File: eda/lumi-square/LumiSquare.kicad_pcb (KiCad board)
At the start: 2 copper layers, 87.2 x 87.2 mm, 105 parts, among them J1 USB_C_Receptacle_USB2.0_14P, J2 Conn_01x12, J3 Conn_01x12, J4 Conn_01x02, J7 FTSH-105-01-X-DV-P-K-X, Q1 IRLML6244, Q10 IRLML2246, Q15 TSM680P06CH, Q16 TSM680P06CH, Q17 TSM680P06CH, Q18 TSM680P06CH, Q2 IRLML2246, Q3 IRLML2246, Q4 MMBT3904, Q5 MMBT3904, Q6 MMBT3904, Q7 MMBT3904, Q8 MMBT3904, Q9 MMBT3904, SW1 SW_SPST, SW2 SW_Push, SW3 SW_Push, SW4 SW_Push, SW5 SW_Push, U1 MCP73831-2-OT, U2 TPS3840, U3 TLV61070A, U4 TLV61070A, U5 ATSAMD21J18A-A, U6 STP16CPC05MTR, U7 CM1224-02SR, U8 MIC5225-3.3YM5, U9 DFR0299

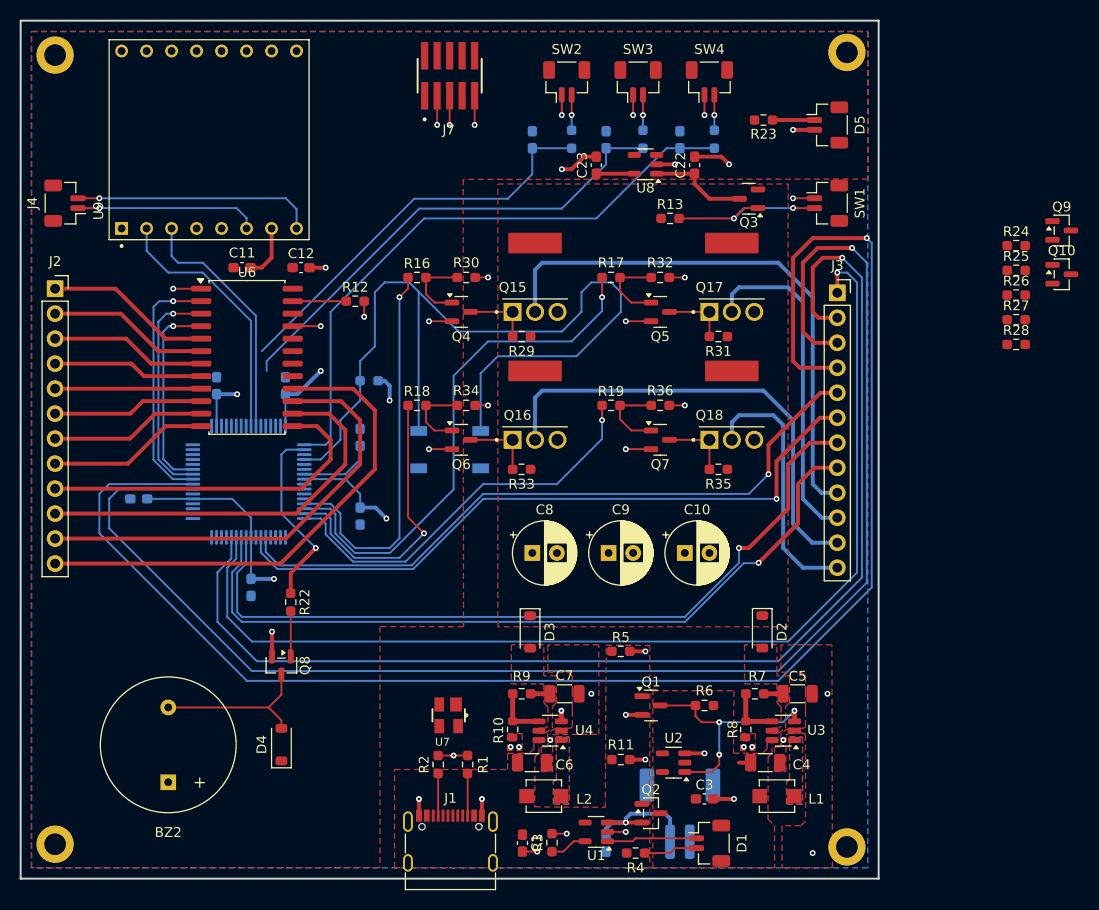
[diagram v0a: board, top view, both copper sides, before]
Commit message: Removed usb connection components and finished circuit
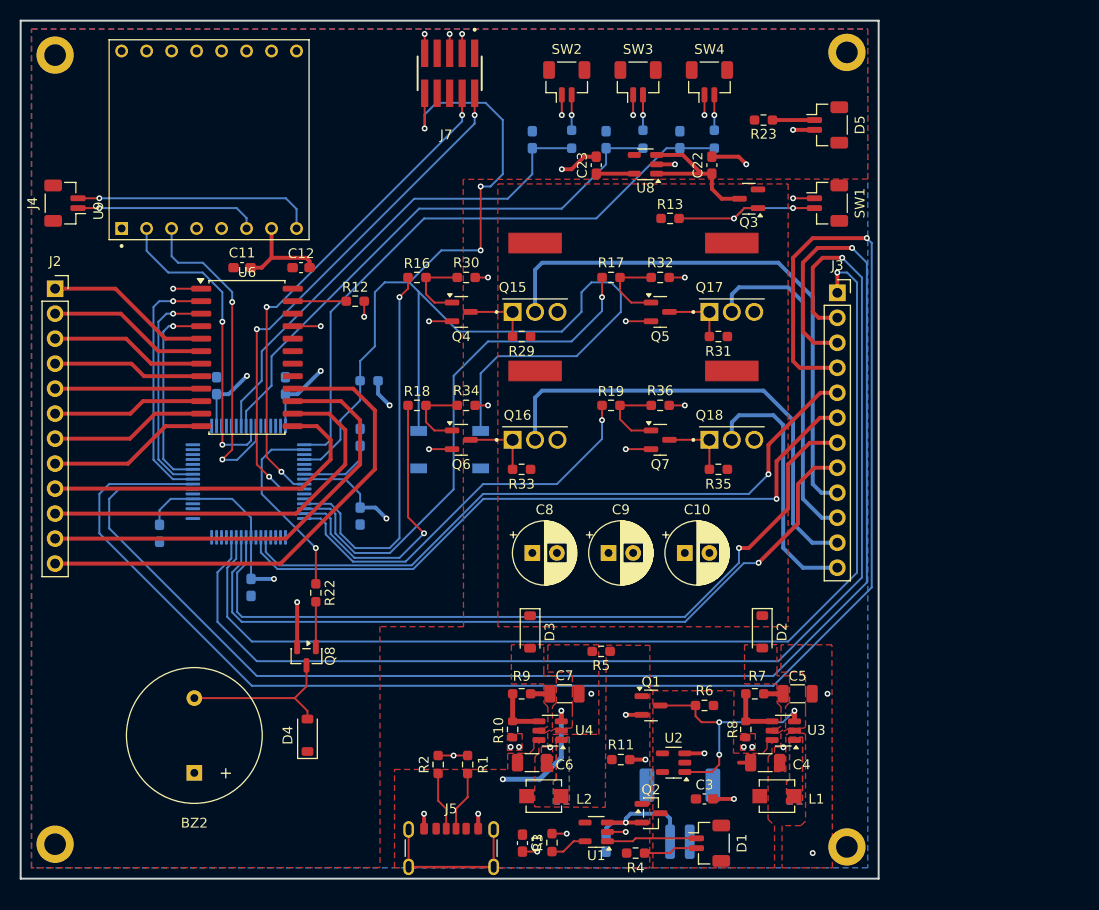
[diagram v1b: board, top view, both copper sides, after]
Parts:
- removed J1: USB_C_Receptacle_USB2.0_14P, Connector_USB:USB_C_Receptacle_G-Switch_GT-USB-7010ASV
- removed Q10: IRLML2246, Package_TO_SOT_SMD:SOT-23
- removed Q9: MMBT3904, Package_TO_SOT_SMD:SOT-23
- removed R24, R25: 1.3k, Resistor_SMD:R_0603_1608Metric_Pad0.98x0.95mm_HandSolder
- removed R26: 33k, Resistor_SMD:R_0603_1608Metric_Pad0.98x0.95mm_HandSolder
- removed R27: 41k, Resistor_SMD:R_0603_1608Metric_Pad0.98x0.95mm_HandSolder
- removed R28: 100k, Resistor_SMD:R_0603_1608Metric_Pad0.98x0.95mm_HandSolder
- removed U7: CM1224-02SR, CM1224-02SR:SOT143
- added J5: USB_C_Receptacle_PowerOnly_6P, Connector_USB:USB_C_Receptacle_GCT_USB4125-xx-x-0190_6P_TopMnt_Horizontal, F.Cu at (144.8, 143.6)
- moved C18 4.09 mm to (115.1, 110.5), turned to -90 degrees
- moved BZ2 2.82 mm to (118.7, 131.1)
- moved D4 2.82 mm to (130.2, 131.0)
- moved Q8 2.72 mm to (130.1, 123.0)
- moved R22 2.72 mm to (131.0, 116.5)
- moved R5 2.00 mm to (160.0, 122.5), turned to 180 degrees
- moved C22 1.75 mm to (171.2, 73.1)
- moved J7 0.25 mm to (144.6, 63.8), turned to 180 degrees
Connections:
- U5 pad 31: /PA14 USB VBUS -> unconnected-(U5-PA14-Pad31)
- U5 pad 45: /TARGET USB N -> unconnected-(U5-PA24-Pad45)
- U5 pad 46: /TARGET USB P -> unconnected-(U5-PA25-Pad46)
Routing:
- net /SWDIO: track 0.00 -> 52.2 mm, vias 0 -> 3
- net /SWCLK: track 0.00 -> 49.5 mm, vias 0 -> 3
- net /Reset Pin: track 90.9 -> 127.2 mm, vias 0 -> 3
- net unconnected-(J5-SHIELD-PadSH): track 0.00 -> 16.2 mm
- net /5V USB: track 1.08 -> 12.7 mm, vias 1 -> 2
- net /MCU RX: track 25.1 -> 33.7 mm, vias 0 -> 2
- net /Previous Btn: track 41.6 -> 50.0 mm
- net Net-(Q3-D): track 10.1 -> 16.8 mm
- net /Next Btn: track 49.2 -> 55.6 mm
- net /MCU TX: track 26.5 -> 31.8 mm, vias 0 -> 2
- net +3.3V Main: track 50.7 -> 52.9 mm
- net Net-(J5-CC2): track 4.29 -> 6.10 mm
- net Net-(J5-CC1): track 4.29 -> 5.95 mm
- net /Buzzer PWM: track 19.1 -> 19.7 mm
- net GNDREF: track 81.5 -> 81.6 mm, vias 44 -> 42

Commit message: Fixed warnings
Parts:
- J4: footprint Connector_JST:JST_SH_BM02B-SRSS-TB_1x02-1MP_P1.00mm_Vertical -> Connector_JST:JST_SH_SM02B-SRSS-TB_1x02-1MP_P1.00mm_Horizontal; moved to B.Cu
- moved J4 30.6 mm to (135.5, 70.8), turned to -90 degrees
- moved J7 0.75 mm to (144.6, 64.5), turned to 0 degrees
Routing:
- net /Speaker-: track 24.6 -> 11.3 mm, vias 1 -> 0
- net GNDREF: track 81.6 -> 91.7 mm
- net /SWCLK: track 49.5 -> 57.2 mm
- net /SWDIO: track 52.2 -> 58.8 mm
- net /Speaker+: track 18.6 -> 16.3 mm, vias 1 -> 0
- net /Reset Pin: track 127.2 -> 126.2 mm
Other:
- board text added: "QB.Creates"
- board text added: "pcb-lumisquare-A1"

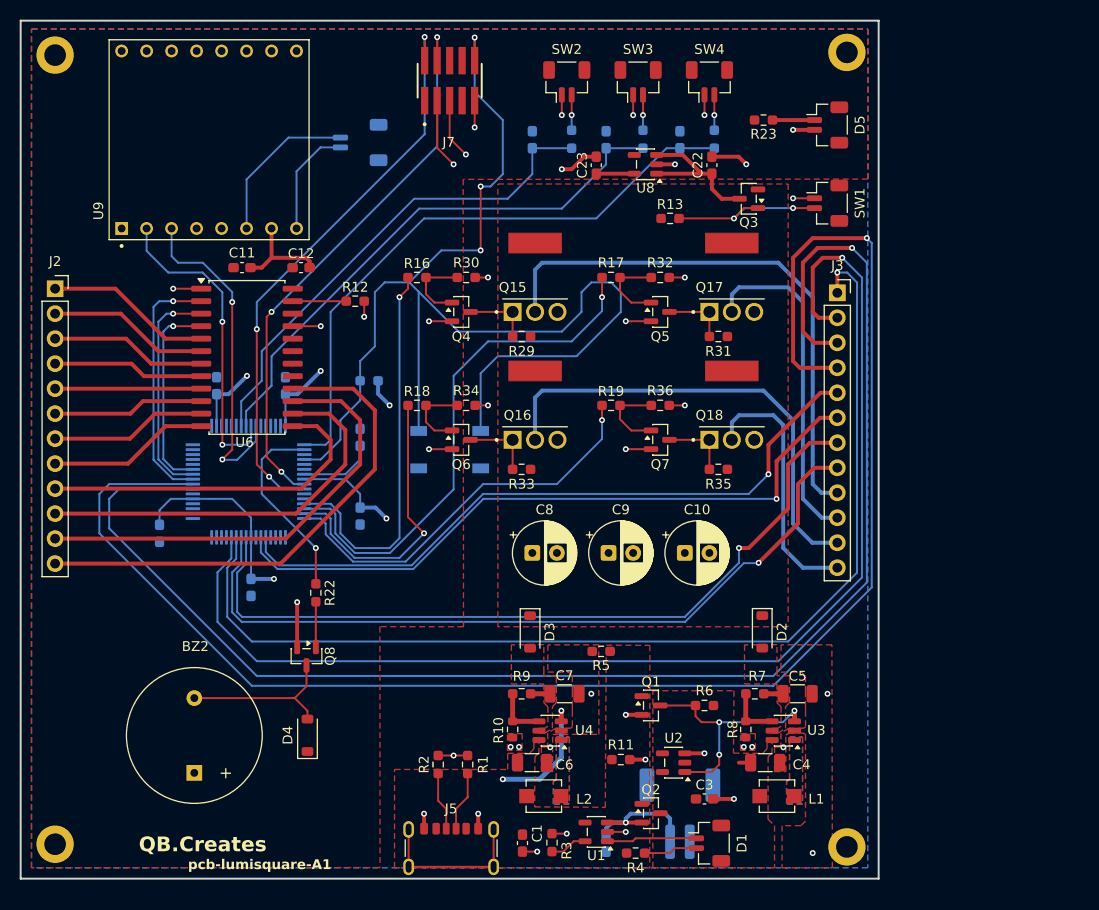
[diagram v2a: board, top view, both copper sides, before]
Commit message: Fixed header positions
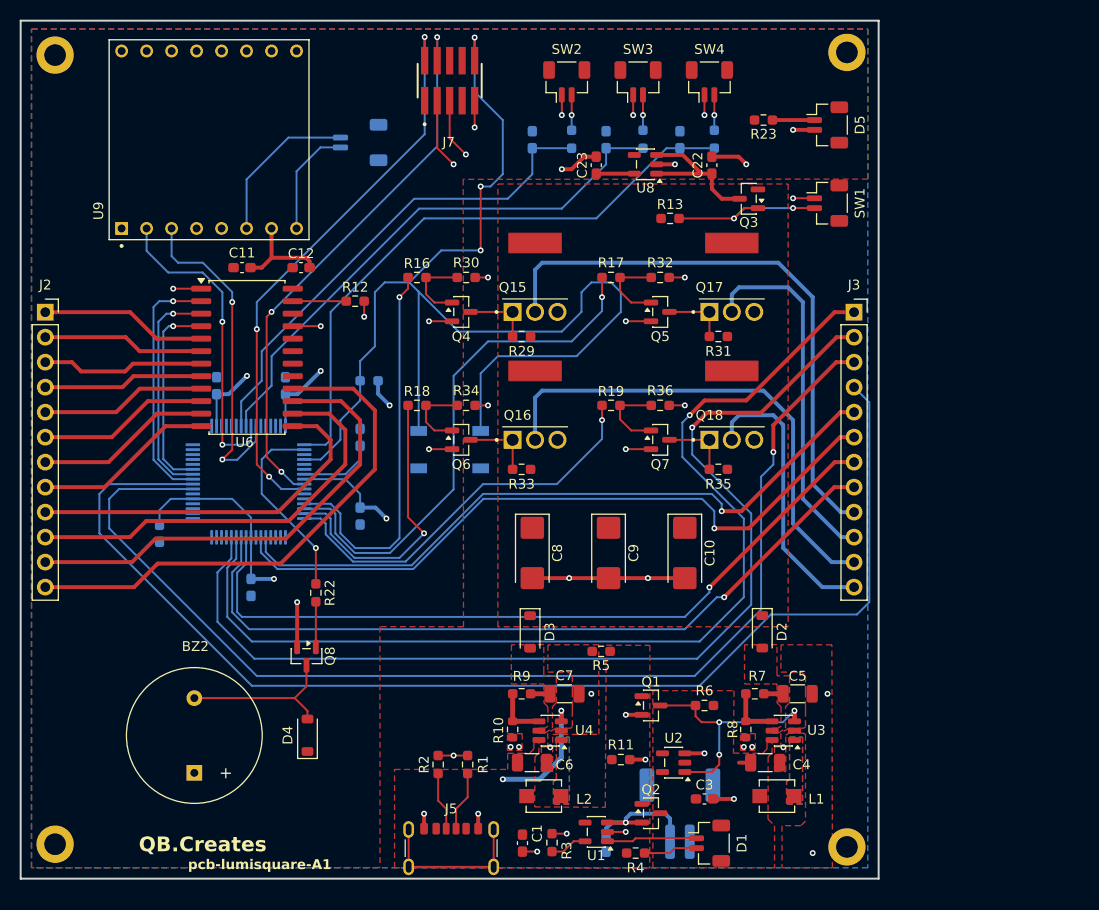
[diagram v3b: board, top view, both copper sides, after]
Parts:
- C10, C8, C9: footprint Capacitor_THT:CP_Radial_D6.3mm_P2.50mm -> Capacitor_Tantalum_SMD:CP_EIA-6032-28_Kemet-C_HandSolder
- moved J3 2.60 mm to (185.7, 88.0)
- moved J2 2.59 mm to (103.5, 88.0)
- turned C10 to -90 degrees
- turned C8 to -90 degrees
- turned C9 to -90 degrees
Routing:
- net /Row/Input 4: track 162.3 -> 124.6 mm, vias 1 -> 0
- net /Row/Input 3: track 150.3 -> 117.3 mm
- net /Row/Input 2: track 123.8 -> 108.0 mm
- net GNDREF: track 91.7 -> 107.2 mm, vias 42 -> 44
- net /Row/Input 1: track 110.4 -> 106.3 mm
- net /Col 3 Anode: track 47.9 -> 50.4 mm
- net /Col 2 Anode: track 34.2 -> 36.7 mm
- net /Col 4 Anode: track 26.5 -> 29.1 mm
- net /Col 1 Anode: track 56.1 -> 58.6 mm
- net /Col/Output 3: track 80.0 -> 77.7 mm
- net Net-(J2-Pin_12): track 51.7 -> 54.0 mm
- net /Col/Output 2: track 69.4 -> 71.6 mm
- net Net-(J2-Pin_11): track 46.3 -> 48.3 mm
- net Net-(J2-Pin_9): track 35.7 -> 37.6 mm
- net Net-(J2-Pin_8): track 16.4 -> 18.4 mm
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
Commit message: Added test points
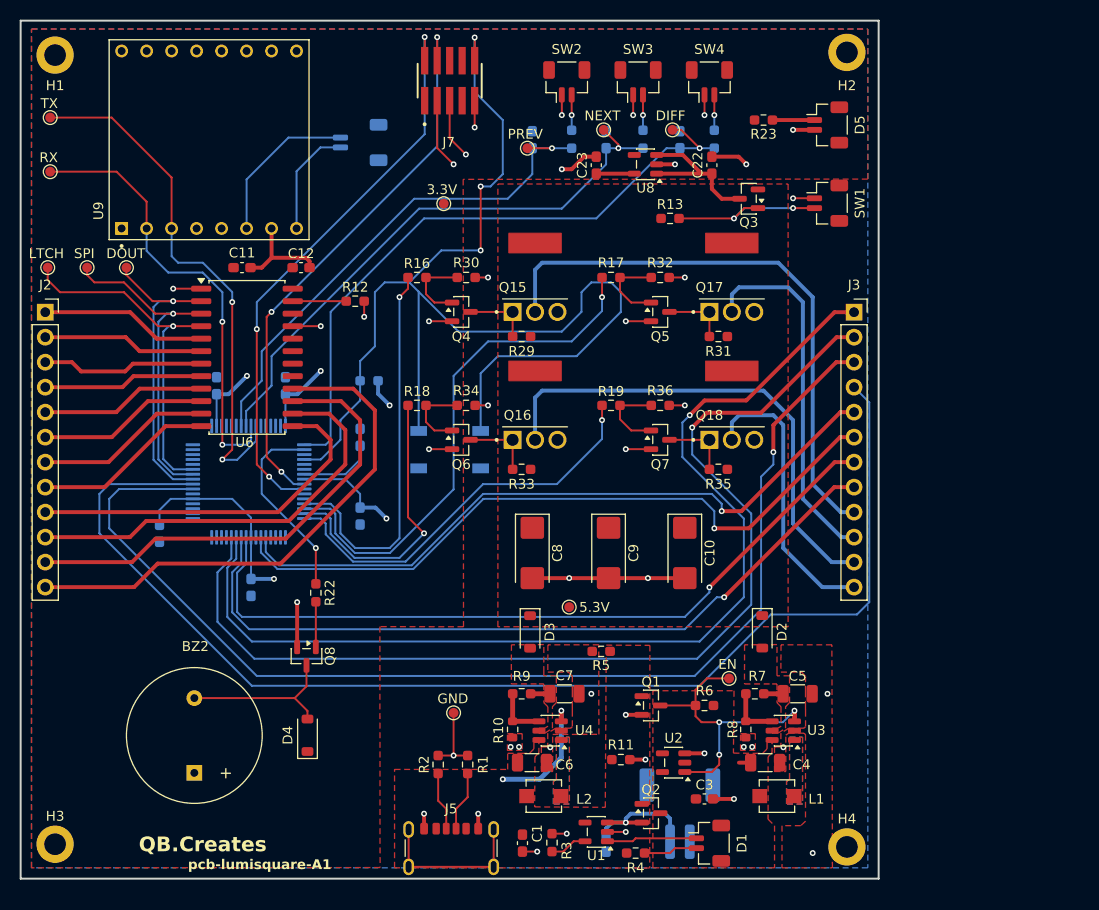
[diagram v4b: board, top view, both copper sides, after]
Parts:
- removed REF** (x4): M2, MountingHole:MountingHole_2.2mm_M2_DIN965_Pad
- added H1: MountingHole, MountingHole:MountingHole_2.2mm_M2_DIN965_Pad, F.Cu at (104.5, 61.9)
- added H2: MountingHole, MountingHole:MountingHole_2.2mm_M2_DIN965_Pad, F.Cu at (185.0, 61.6)
- added H3: MountingHole, MountingHole:MountingHole_2.2mm_M2_DIN965_Pad, F.Cu at (104.5, 142.1)
- added H4: MountingHole, MountingHole:MountingHole_2.2mm_M2_DIN965_Pad, F.Cu at (185.0, 142.4)
- added J1: Conn_01x01, TestPoint:TestPoint_Pad_D1.0mm, F.Cu at (156.8, 118.0)
- added J10: Conn_01x01, TestPoint:TestPoint_Pad_D1.0mm, F.Cu at (152.5, 71.4)
- added J11: Conn_01x01, TestPoint:TestPoint_Pad_D1.0mm, F.Cu at (160.2, 69.5)
- added J12: Conn_01x01, TestPoint:TestPoint_Pad_D1.0mm, F.Cu at (167.2, 69.5)
- added J13: Conn_01x01, TestPoint:TestPoint_Pad_D1.0mm, F.Cu at (104.0, 73.8)
- added J14: Conn_01x01, TestPoint:TestPoint_Pad_D1.0mm, F.Cu at (104.0, 68.2)
- added J15: Conn_01x01, TestPoint:TestPoint_Pad_D1.0mm, F.Cu at (111.8, 83.5)
- added J16: Conn_01x01, TestPoint:TestPoint_Pad_D1.0mm, F.Cu at (107.8, 83.5)
- added J17: Conn_01x01, TestPoint:TestPoint_Pad_D1.0mm, F.Cu at (103.8, 83.5)
- added J6: Conn_01x01, TestPoint:TestPoint_Pad_D1.0mm, F.Cu at (173.0, 125.2)
- added J8: Conn_01x01, TestPoint:TestPoint_Pad_D1.0mm, F.Cu at (145.0, 128.8)
- added J9: Conn_01x01, TestPoint:TestPoint_Pad_D1.0mm, F.Cu at (144.0, 77.0)
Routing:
- net /MCU RX: track 33.7 -> 53.7 mm
- net /SPI Latch: track 20.5 -> 36.4 mm
- net /MCU TX: track 31.8 -> 45.6 mm
- net /SPI CLK: track 22.8 -> 33.9 mm
- net /SPI Dout: track 25.4 -> 32.0 mm
- net Net-(J6-Pin_1): track 24.7 -> 30.2 mm
- net GNDREF: track 107.2 -> 111.6 mm
- net /Difficulty Btn: track 61.8 -> 65.3 mm, vias 0 -> 1
- net /Previous Btn: track 50.0 -> 52.5 mm, vias 0 -> 1
- net /Next Btn: track 55.6 -> 58.1 mm, vias 0 -> 1
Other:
- board text added: "3.3V"
- board text added: "5.3V"
- board text added: "DIFF"
- board text added: "DOUT"
- board text added: "EN"
- board text added: "GND"
- board text added: "LTCH"
- board text added: "NEXT"
- board text added: "PREV"
- board text added: "RX"
- board text added: "SPI"
- board text added: "TX"
